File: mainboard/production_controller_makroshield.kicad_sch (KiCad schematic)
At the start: 48 parts, among them J1 CON_TERM_BLK_1X2_TB008A-508-0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, J2 CON_TERM_BLK_1X2_TB008A-508-0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, J3 CON_HDR_MIKROBUS_ADDON_TH, J4 CON_TERM_BLK_1X2_TB008A-508-0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, J5 CON_HDR_MIKROBUS_SOCKET_TH, Q1 TRX_PMOS_AOD4189, Q2 TRX_NPN_MMBT3904-TP, U1 IO_EXP_PI4IOE5V6416ZDEX, U2 IO_EXP_PI4IOE5V6416ZDEX, U3 SUN_CUR_ACS711KEXLT-31AB-T, U4 ADC_NAU7802SGI

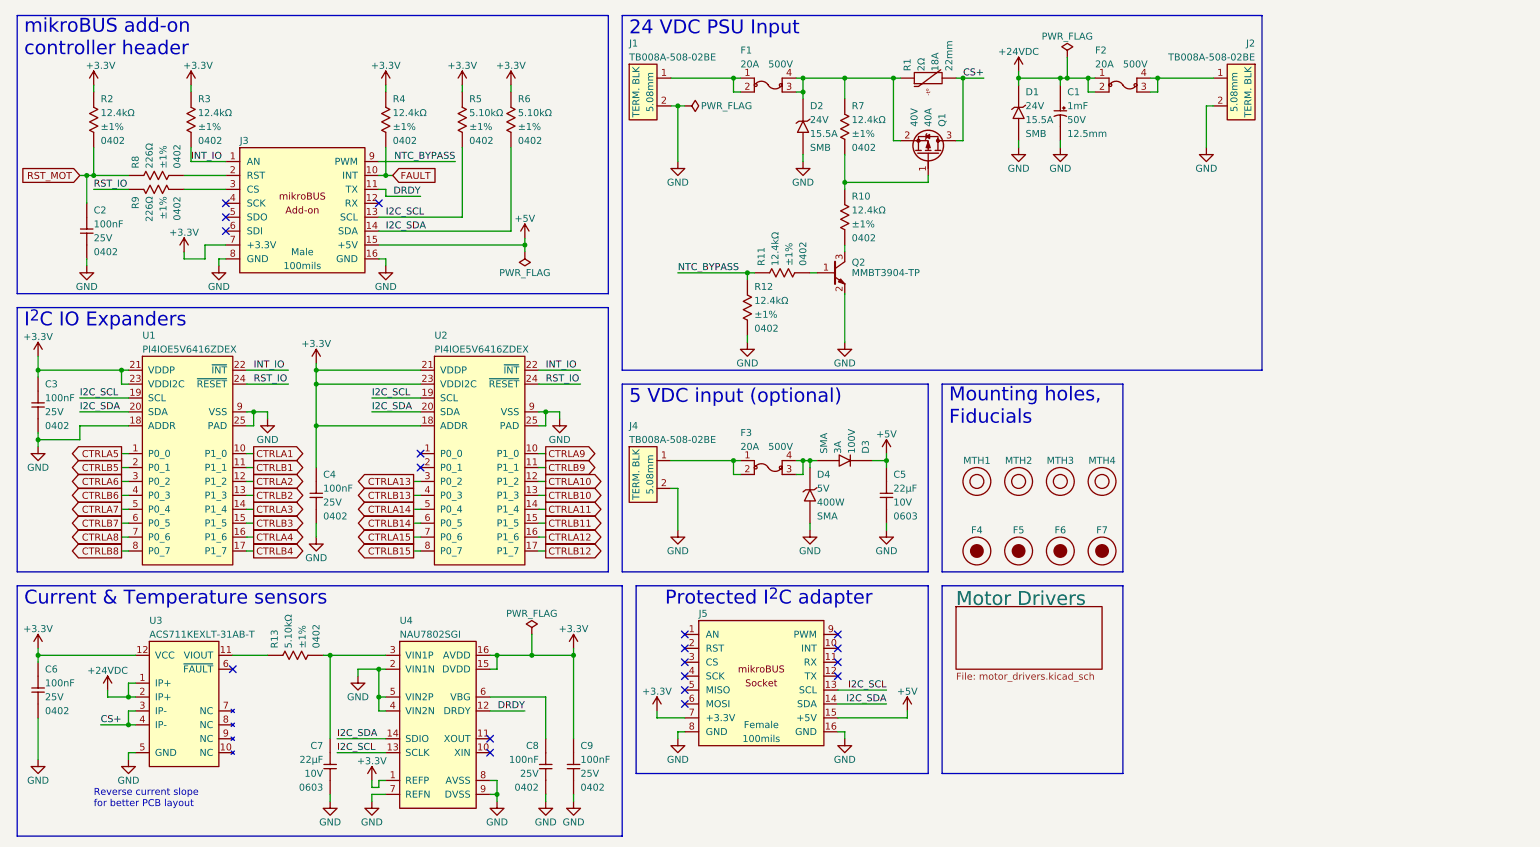
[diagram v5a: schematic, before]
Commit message: Add high-current pathways and extra capacitors. DRC pass
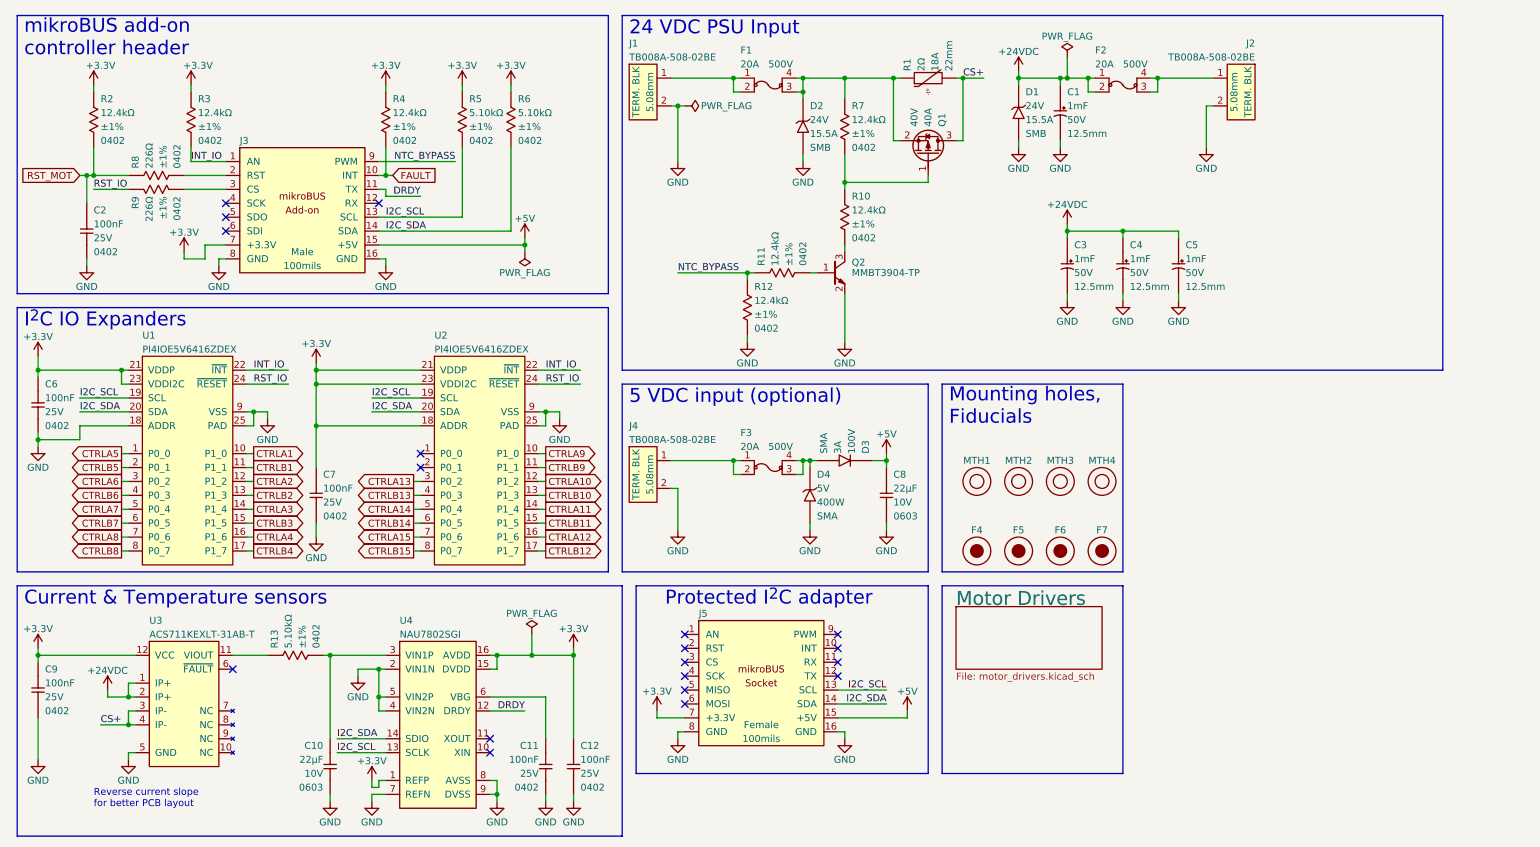
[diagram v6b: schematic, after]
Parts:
- added C3, C4, C5: CAP_AE_1MF_50V_TH_12.5MM, connaxio-capacitors:CAPAE_RAD_D12.5_H26.5_P5, symbol connaxio-capacitors:CAP_AE_1MF_50V_TH_12.5MM
- renumbered C7 to C10, C8 to C11, C9 to C12, C3 to C6, C4 to C7, C5 to C8, C6 to C9
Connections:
- net +24VDC: now also C3.1, C4.1, C5.1
- net GND: now also C3.2, C4.2, C5.2

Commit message: Add LEDs, fix NMOS, Add logos and infos on PCBs.
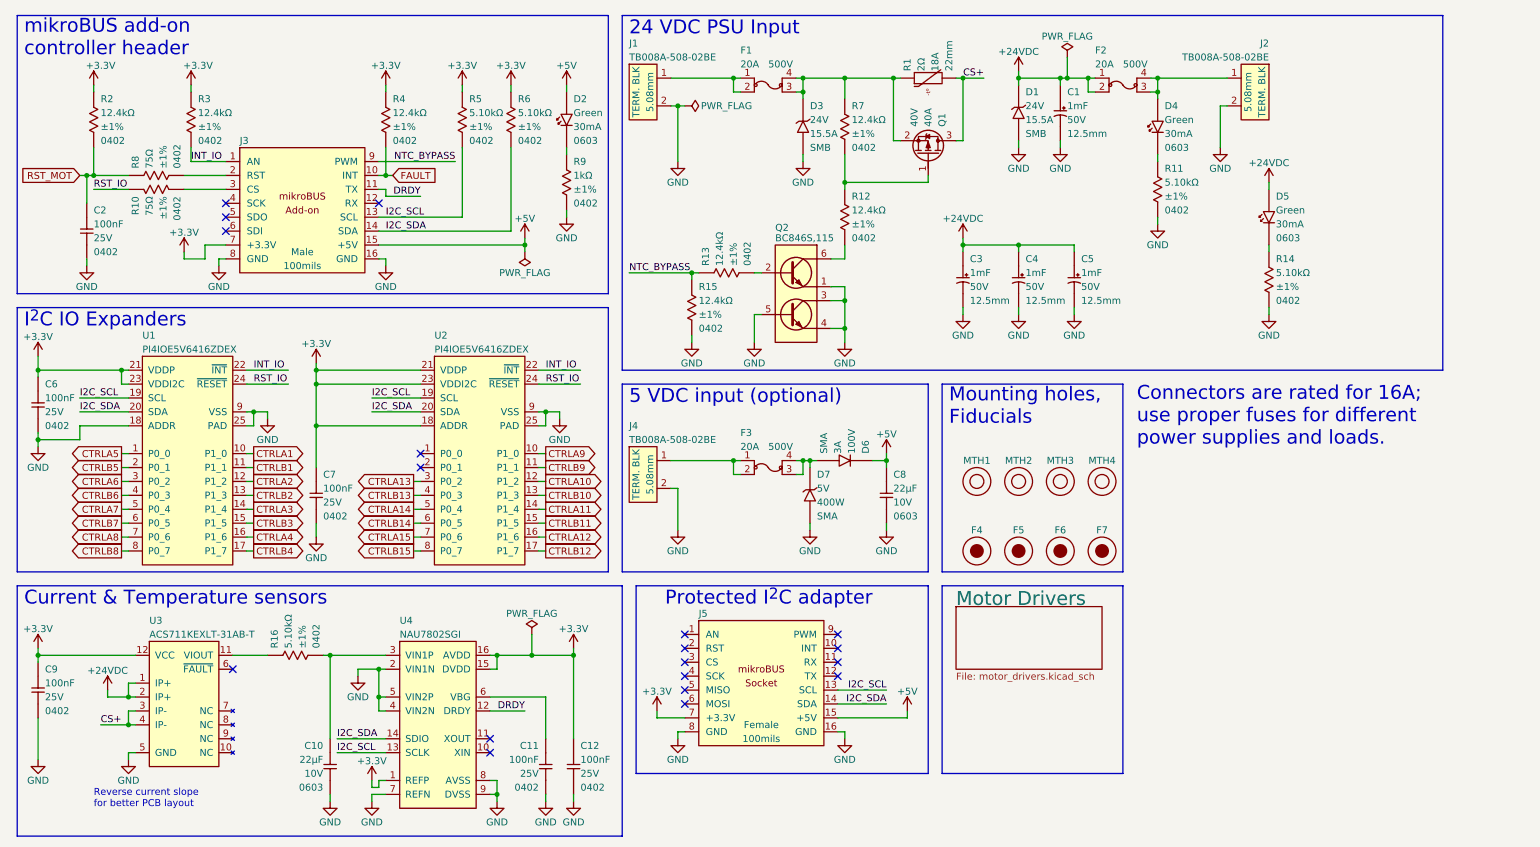
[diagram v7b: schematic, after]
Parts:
- removed Q2: TRX_NPN_MMBT3904-TP, connaxio-sop:SOT-23-3, symbol connaxio-transistors:TRX_NPN_MMBT3904-TP
- added D2, D4, D5: DIO_LED_GREEN_150060GS75000, connaxio-diodes:LED_0603_1608M, symbol connaxio-diodes:DIO_LED_GREEN_150060GS75000
- added Q2: TRX_2NPN_BC846S,115, connaxio-sop:SOT-363_SC-70-6, symbol connaxio-transistors:TRX_2NPN_BC846S,115
- added R11, R14: RES_5.10KΩ_1%_0402, connaxio-resistors:RES_0402_1005M, symbol connaxio-resistors:RES_5.10KΩ_1%_0402
- added R9: RES_1.00KΩ_1%_0402, connaxio-resistors:RES_0402_1005M, symbol connaxio-resistors:RES_1.00KΩ_1%_0402
- R10: renamed from R9; symbol connaxio-resistors:RES_226Ω_1%_0402 -> connaxio-resistors:RES_75Ω_1%_0402; Manufacturer Part Number RMCF0402FT226R -> RMCF0402FT75R0; Property 226Ω -> 75Ω
- R8: symbol connaxio-resistors:RES_226Ω_1%_0402 -> connaxio-resistors:RES_75Ω_1%_0402; Manufacturer Part Number RMCF0402FT226R -> RMCF0402FT75R0; Property 226Ω -> 75Ω
- renumbered D2 to D3, D3 to D6, D4 to D7, R10 to R12, R11 to R13, R12 to R15, R13 to R16
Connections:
- net +24VDC: now also D5.2 (A)
- net +5V: now also D2.2 (A)
- net GND: now also Q2.1 (E1), Q2.3 (C2), Q2.4 (E2), Q2.5 (B2), R11.2, R14.2, R9.2
- net at R13.2: now also Q2.2 (B1)
- net at R12.2: now also Q2.6 (C1)
- net at F2.3, F2.4, J2.1: now also D4.2 (A)
- new net: D4.1 (K), R11.1
- new net: D5.1 (K), R14.1
- new net: D2.1 (K), R9.1
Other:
- note added: "Connectors are rated for 16A; use proper fuses for different power supplies and loads."
- moved on the sheet: C3, C4, C5, J2, R13, R15

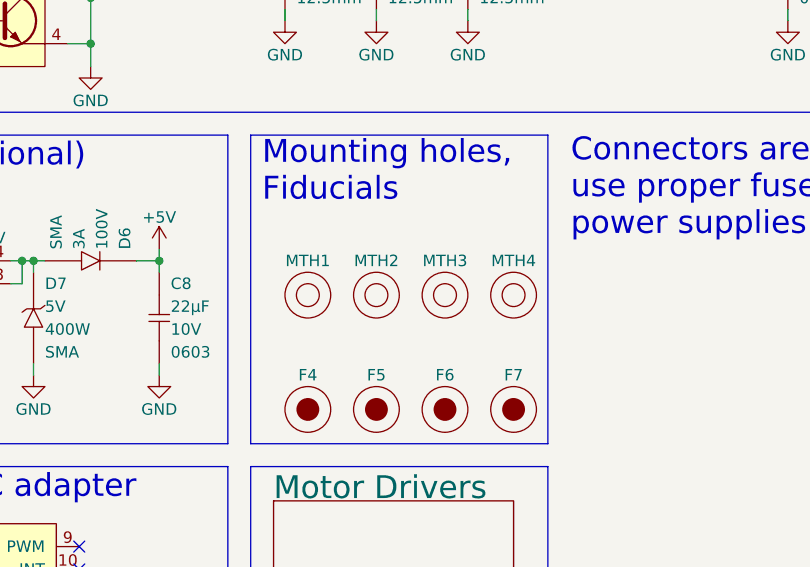
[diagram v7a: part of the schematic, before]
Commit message: Add Enclosure piercing guide and fix h-bridge-driver NMOS pads.
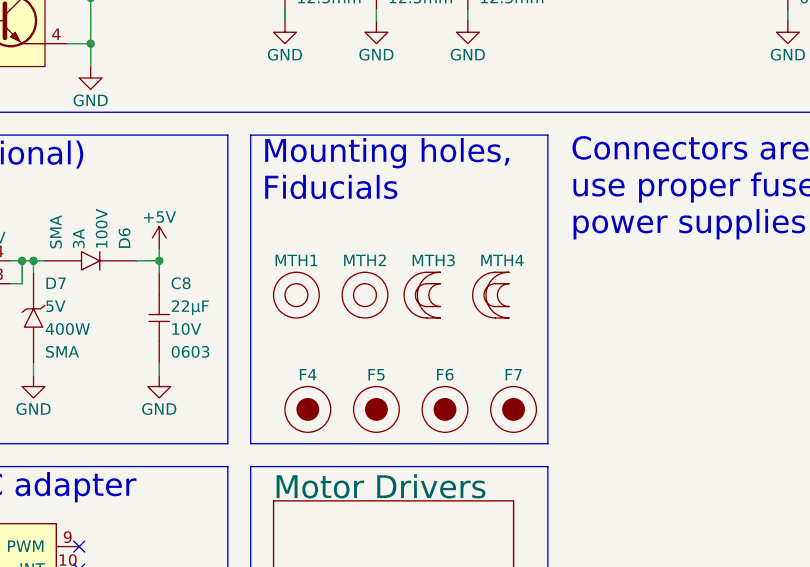
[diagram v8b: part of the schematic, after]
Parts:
- removed MTH3, MTH4: MTH_M5_NPTH, connaxio-mechanical:MTH_M5_NPTH, symbol connaxio-mechanical:MTH_M5_NPTH
- added MTH3, MTH4: MTH_SLOT_M5_2MM_NPTH, connaxio-mechanical:MTH_SLOT_M5_2MM_NPTH, symbol connaxio-mechanical:MTH_SLOT_M5_2MM_NPTH
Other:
- moved on the sheet: MTH1, MTH2
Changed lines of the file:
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@@
     (pin "1")
   )
+  (symbol (lib_id "connaxio-mechanical:MTH_SLOT_M5_2MM_NPTH") (at 212.09 100.33 0) (unit 1)
+    (in_bom no) (on_board yes)
+    (property "Reference" "MTH4" (id 0) (at 212.09 96.52 0))
+    (property "Value" "MTH_SLOT_M5_2MM_NPTH" (id 1) (at 218.44 93.98 0)
+      (effects (font (size 1.27 1.27)) hide)
+    )
+    (property "Footprint" "connaxio-mechanical:MTH_SLOT_M5_2MM_NPTH" (id 2) (at 221.615 92.075 0)
+      (effects (font (size 1.27 1.27)) hide)
+    )
+    (property "Datasheet" "" (id 3) (at 212.09 99.06 0)
+      (effects (font (size 1.27 1.27)) hide)
+    )
+    (property "Property" "5.5mm" (id 4) (at 205.74 94.742 0)
+      (effects (font (size 1.27 1.27)) hide)
+    )
+  )
   (symbol (lib_id "connaxio-mechanical:FID_1X3") (at 205.74 113.03 0) (unit 1)
     (in_bom no) (on_board yes)
@@
     (pin "4")
   )
-  (symbol (lib_id "connaxio-mechanical:MTH_M5_NPTH") (at 213.36 100.33 0) (unit 1)
-    (in_bom no) (on_board yes)
-    (property "Reference" "MTH4" (id 0) (at 213.36 96.52 0))
-    (property "Value" "MTH_M5_NPTH" (id 1) (at 219.71 93.98 0)
-      (effects (font (size 1.27 1.27)) hide)
-    )
-    (property "Footprint" "connaxio-mechanical:MTH_M5_NPTH" (id 2) (at 222.885 92.075 0)
-      (effects (font (size 1.27 1.27)) hide)
-    )
-    (property "Datasheet" "" (id 3) (at 213.36 99.06 0)
-      (effects (font (size 1.27 1.27)) hide)
-    )
-    (property "Property" "5.5mm" (id 4) (at 213.36 100.33 0)
-      (effects (font (size 1.27 1.27)) hide)
-    )
-  )
   (symbol (lib_id "power:GND") (at 223.52 53.34 0) (unit 1)
     (in_bom yes) (on_board yes)
@@
     (pin "1")
   )
+  (symbol (lib_id "connaxio-mechanical:MTH_SLOT_M5_2MM_NPTH") (at 204.47 100.33 0) (unit 1)
+    (in_bom no) (on_board yes)
+    (property "Reference" "MTH3" (id 0) (at 204.47 96.52 0))
+    (property "Value" "MTH_SLOT_M5_2MM_NPTH" (id 1) (at 210.82 93.98 0)
+      (effects (font (size 1.27 1.27)) hide)
+    )
+    (property "Footprint" "connaxio-mechanical:MTH_SLOT_M5_2MM_NPTH" (id 2) (at 213.995 92.075 0)
+      (effects (font (size 1.27 1.27)) hide)
+    )
+    (property "Datasheet" "" (id 3) (at 204.47 99.06 0)
+      (effects (font (size 1.27 1.27)) hide)
+    )
+    (property "Property" "5.5mm" (id 4) (at 198.12 94.742 0)
+      (effects (font (size 1.27 1.27)) hide)
+    )
+  )
   (symbol (lib_id "connaxio-resistors:RES_5.10KΩ_1%_0402") (at 223.52 46.99 0) (unit 1)
     (in_bom yes) (on_board yes)
@@
     (pin "1")
   )
-  (symbol (lib_id "connaxio-mechanical:MTH_M5_NPTH") (at 198.12 100.33 0) (unit 1)
+  (symbol (lib_id "connaxio-mechanical:MTH_M5_NPTH") (at 196.85 100.33 0) (unit 1)
     (in_bom no) (on_board yes)
-    (property "Reference" "MTH2" (id 0) (at 198.12 96.52 0))
-    (property "Value" "MTH_M5_NPTH" (id 1) (at 204.47 93.98 0)
+    (property "Reference" "MTH2" (id 0) (at 196.85 96.52 0))
+    (property "Value" "MTH_M5_NPTH" (id 1) (at 203.2 93.98 0)
       (effects (font (size 1.27 1.27)) hide)
     )
-    (property "Footprint" "connaxio-mechanical:MTH_M5_NPTH" (id 2) (at 207.645 92.075 0)
+    (property "Footprint" "connaxio-mechanical:MTH_M5_NPTH" (id 2) (at 206.375 92.075 0)
       (effects (font (size 1.27 1.27)) hide)
     )
-    (property "Datasheet" "" (id 3) (at 198.12 99.06 0)
+    (property "Datasheet" "" (id 3) (at 196.85 99.06 0)
       (effects (font (size 1.27 1.27)) hide)
     )
-    (property "Property" "5.5mm" (id 4) (at 198.12 100.33 0)
+    (property "Property" "5.5mm" (id 4) (at 196.85 100.33 0)
       (effects (font (size 1.27 1.27)) hide)
     )
@@
     )
   )
-  (symbol (lib_id "connaxio-mechanical:MTH_M5_NPTH") (at 190.5 100.33 0) (unit 1)
+  (symbol (lib_id "connaxio-mechanical:MTH_M5_NPTH") (at 189.23 100.33 0) (unit 1)
     (in_bom no) (on_board yes)
-    (property "Reference" "MTH1" (id 0) (at 190.5 96.52 0))
-    (property "Value" "MTH_M5_NPTH" (id 1) (at 196.85 93.98 0)
+    (property "Reference" "MTH1" (id 0) (at 189.23 96.52 0))
+    (property "Value" "MTH_M5_NPTH" (id 1) (at 195.58 93.98 0)
       (effects (font (size 1.27 1.27)) hide)
     )
-    (property "Footprint" "connaxio-mechanical:MTH_M5_NPTH" (id 2) (at 200.025 92.075 0)
+    (property "Footprint" "connaxio-mechanical:MTH_M5_NPTH" (id 2) (at 198.755 92.075 0)
       (effects (font (size 1.27 1.27)) hide)
     )
-    (property "Datasheet" "" (id 3) (at 190.5 99.06 0)
+    (property "Datasheet" "" (id 3) (at 189.23 99.06 0)
       (effects (font (size 1.27 1.27)) hide)
     )
-    (property "Property" "5.5mm" (id 4) (at 190.5 100.33 0)
+    (property "Property" "5.5mm" (id 4) (at 189.23 100.33 0)
       (effects (font (size 1.27 1.27)) hide)
     )
@@
     )
   )
-  (symbol (lib_id "connaxio-mechanical:MTH_M5_NPTH") (at 205.74 100.33 0) (unit 1)
-    (in_bom no) (on_board yes)
-    (property "Reference" "MTH3" (id 0) (at 205.74 96.52 0))
-    (property "Value" "MTH_M5_NPTH" (id 1) (at 212.09 93.98 0)
-      (effects (font (size 1.27 1.27)) hide)
-    )
-    (property "Footprint" "connaxio-mechanical:MTH_M5_NPTH" (id 2) (at 215.265 92.075 0)
-      (effects (font (size 1.27 1.27)) hide)
-    )
-    (property "Datasheet" "" (id 3) (at 205.74 99.06 0)
-      (effects (font (size 1.27 1.27)) hide)
-    )
-    (property "Property" "5.5mm" (id 4) (at 205.74 100.33 0)
-      (effects (font (size 1.27 1.27)) hide)
-    )
-  )
   (symbol (lib_id "power:GND") (at 82.55 60.96 0) (unit 1)
     (in_bom yes) (on_board yes)
@@
       (reference "MTH2") (unit 1) (value "MTH_M5_NPTH") (footprint "connaxio-mechanical:MTH_M5_NPTH")
     )
-    (path "/c5db39a2-46c0-401f-8858-19a69ca0e8dc"
-      (reference "MTH3") (unit 1) (value "MTH_M5_NPTH") (footprint "connaxio-mechanical:MTH_M5_NPTH")
+    (path "/3911f39f-d78c-4cbe-809d-053afc53393e"
+      (reference "MTH3") (unit 1) (value "MTH_SLOT_M5_2MM_NPTH") (footprint "connaxio-mechanical:MTH_SLOT_M5_2MM_NPTH")
     )
-    (path "/2e38c119-bb9f-4413-9de7-4f0cb48e36e5"
-      (reference "MTH4") (unit 1) (value "MTH_M5_NPTH") (footprint "connaxio-mechanical:MTH_M5_NPTH")
+    (path "/21fd2965-3ff8-495c-a5f3-0a3be56f4dcf"
+      (reference "MTH4") (unit 1) (value "MTH_SLOT_M5_2MM_NPTH") (footprint "connaxio-mechanical:MTH_SLOT_M5_2MM_NPTH")
     )
     (path "/b33ac4cf-31da-4921-85f6-bc5854baade2"
